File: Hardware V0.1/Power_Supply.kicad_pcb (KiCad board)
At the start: 2 copper layers, 100 x 50 mm, 65 parts, among them J1 ICSP, J2 Conn_01x01, J3 Conn_01x01, J4 Screw_Terminal_01x02, J6 Conn_01x04, J7 Conn_01x04, SW1 UP, SW2 DW, SW3 V/I, SW4 O_EN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

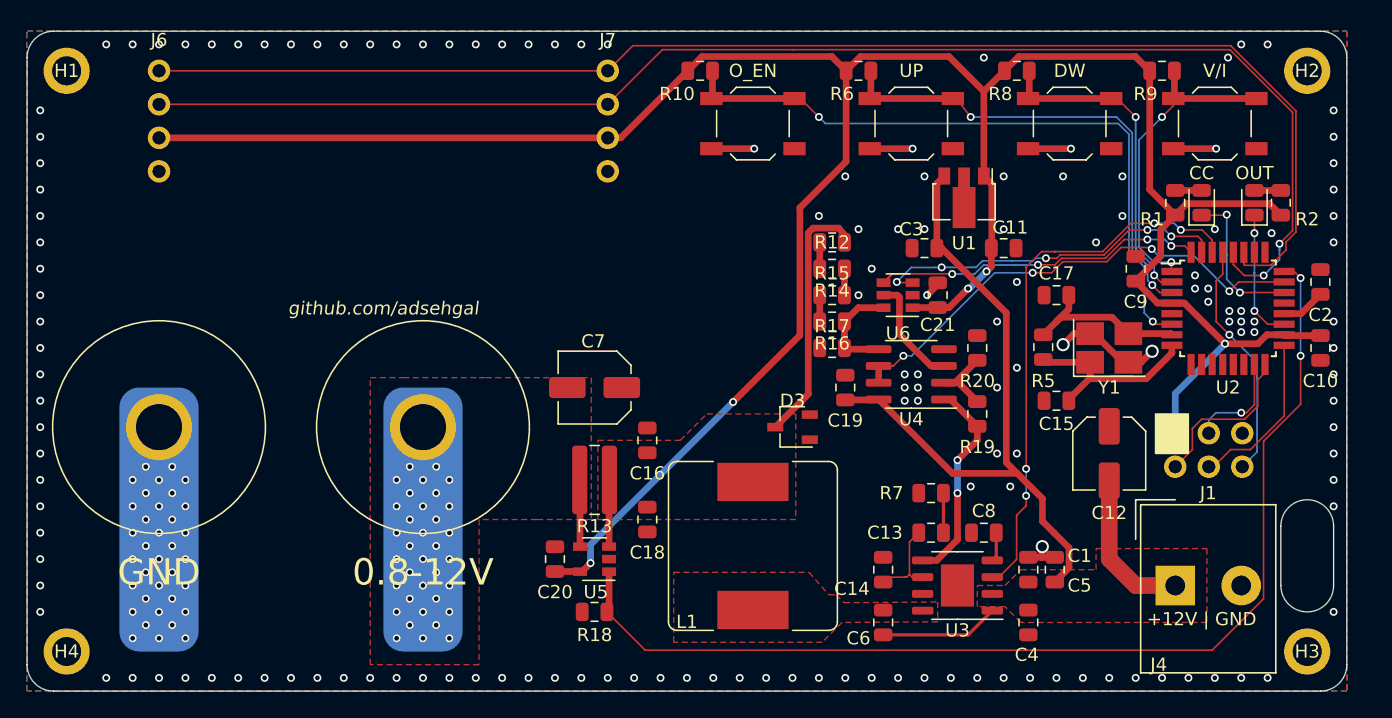
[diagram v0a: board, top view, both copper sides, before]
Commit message: placed all components
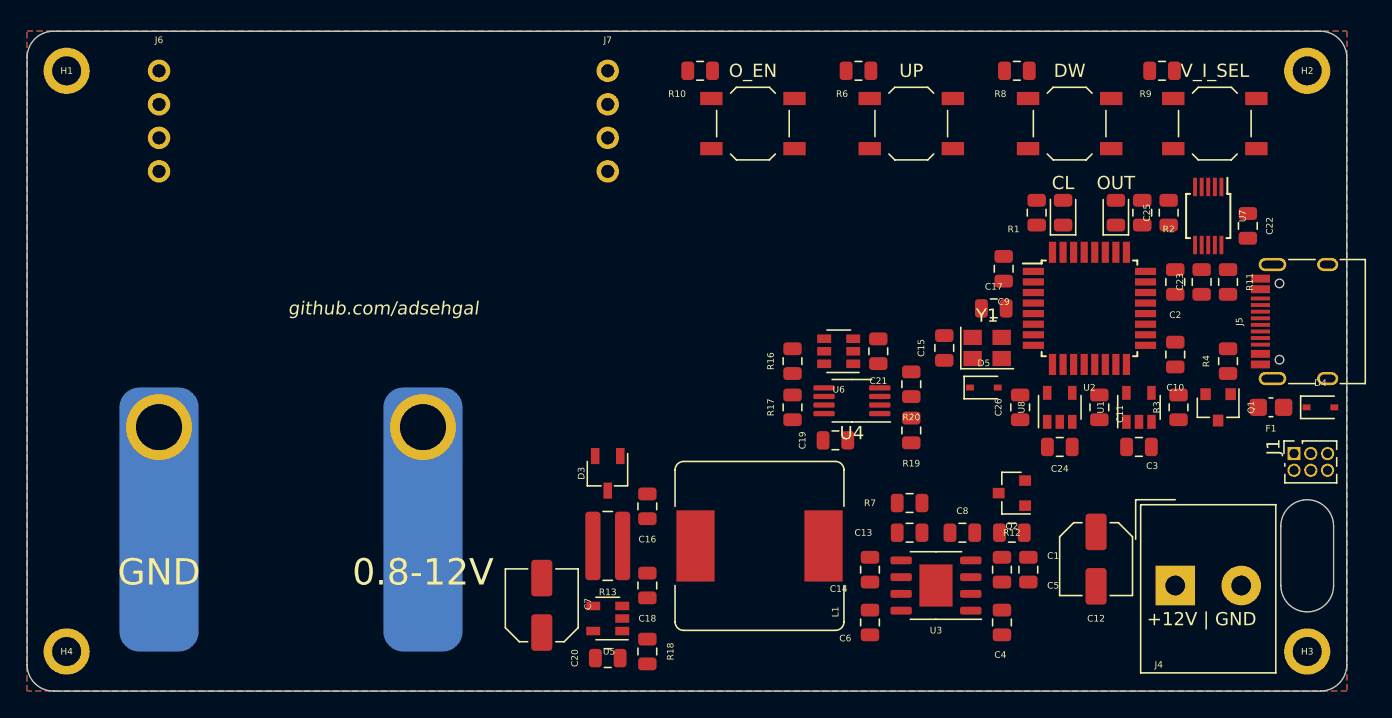
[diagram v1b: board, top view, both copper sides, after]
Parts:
- removed the G*** at (39.0, 29.0) (x2)
- removed R14, R15: 1.5K, Resistor_SMD:R_0805_2012Metric
- removed R5: 1M, Resistor_SMD:R_0805_2012Metric
- added C22: 100nF, Capacitor_SMD:C_0805_2012Metric, F.Cu at (104.5, 26.8)
- added C23: 100nF, Capacitor_SMD:C_0805_2012Metric, F.Cu at (101.0, 31.0)
- added C24: 100nF, Capacitor_SMD:C_0805_2012Metric, F.Cu at (90.2, 43.5)
- added C25: 100nF, Capacitor_SMD:C_0805_2012Metric, F.Cu at (98.5, 25.8)
- added C26: 1µF, Capacitor_SMD:C_0805_2012Metric, F.Cu at (87.2, 40.5)
- added D4: CUS10S30, Diode_SMD:D_SOD-323, F.Cu at (110.0, 40.5)
- added D5: CUS10S30, Diode_SMD:D_SOD-323, F.Cu at (84.5, 39.0)
- added F1: MF-PSMF020X-2, Fuse:Fuse_0805_2012Metric_Castellated, F.Cu at (106.2, 40.5)
- added G***: LOGO, LOGO, F.Cu at (39.5, 29.0)
- added J5: USB_C_Receptacle_USB2.0, Connector_USB:USB_C_Receptacle_HRO_TYPE-C-31-M-12, F.Cu at (109.5, 34.0)
- added Q1: FDN335N, Package_TO_SOT_SMD:SOT-23, F.Cu at (102.2, 40.5)
- added Q2: FDN335N, Package_TO_SOT_SMD:SOT-23, F.Cu at (86.6, 47.0)
- added R11: 5.1K, Resistor_SMD:R_0805_2012Metric, F.Cu at (103.0, 31.0)
- added R3: 10K, Resistor_SMD:R_0805_2012Metric, F.Cu at (99.2, 40.5)
- added R4: 5.1K, Resistor_SMD:R_0805_2012Metric, F.Cu at (103.0, 37.0)
- added U7: CH340E, Package_SO:MSOP-10_3x3mm_P0.5mm, F.Cu at (101.5, 26.0)
- added U8: MIC5205-3.3YM5, Package_TO_SOT_SMD:SOT-23-5, F.Cu at (90.2, 40.5)
- C11: value 100nF -> 1µF
- C20: value C_Small -> 100nF
- D1: value CC -> CL
- J1: footprint Custom_Vertical_2x_2.54mm_Pin_Header:PinHeader_2x03_P2.54mm_Vertical -> Connector_PinSocket_1.27mm:PinSocket_2x03_P1.27mm_Vertical
- R12: value 1K -> 10K
- R16: value 10K -> 14K
- SW3: value V/I -> V_I_SEL
- U1: value L78L08_SOT89 -> MIC5205-5.0YM5; footprint Package_TO_SOT_SMD:SOT-89-3 -> Package_TO_SOT_SMD:SOT-23-5
- U4: footprint Package_SO:SOIC-8_3.9x4.9mm_P1.27mm -> Package_SO:MSOP-8_3x3mm_P0.65mm
- Y1: footprint Crystal:Crystal_SMD_SeikoEpson_TSX3225-4Pin_3.2x2.5mm_HandSoldering -> Crystal:Crystal_SMD_SeikoEpson_TSX3225-4Pin_3.2x2.5mm
- moved R12 25.9 mm to (86.6, 50.0)
- moved C3 22.2 mm to (96.2, 43.5), turned to 180 degrees
- moved U1 20.7 mm to (96.2, 40.5), turned to 90 degrees
- moved C7 17.0 mm to (51.0, 55.5), turned to 90 degrees
- moved D3 14.4 mm to (56.0, 45.5), turned to -90 degrees
- moved C11 14.1 mm to (93.2, 40.5), turned to 90 degrees
- moved C10 11.0 mm to (99.0, 36.5)
- moved C2 11.0 mm to (99.0, 31.0)
- moved D1 10.5 mm to (90.5, 25.8)
- moved D2 10.5 mm to (94.5, 25.8)
- moved R1 10.5 mm to (88.5, 25.8)
- moved R2 10.5 mm to (96.5, 25.8)
- moved U2 10.5 mm to (92.5, 33.0)
- moved C9 10.0 mm to (86.0, 30.0)
- moved C15 9.39 mm to (81.5, 36.0), turned to -90 degrees
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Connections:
- R12 pad 1: Net-(R12-Pad1) -> Net-(Q2-Pad3)
- R12 pad 2: Net-(C16-Pad2) -> +VSW
- R16 pad 2: Net-(R15-Pad1) -> Net-(C16-Pad2)
- U1 pad 1: +5V -> +VSW
- U1 pad 3: +VSW -> Net-(Q1-Pad3)
- U2 pad 10: Net-(U2-Pad10) -> /POT_U~D
- U2 pad 11: Net-(U2-Pad11) -> /~POT_CS
- U2 pad 12: Net-(U2-Pad12) -> (no net)
- U2 pad 13: Net-(U2-Pad13) -> (no net)
- U2 pad 14: /~SS -> (no net)
- U2 pad 25: Net-(U2-Pad25) -> (no net)
- U2 pad 26: Net-(U2-Pad26) -> (no net)
- U2 pad 30: /REG_EN -> /RX
- U2 pad 31: /POT_U~D -> /TX
- U2 pad 32: /~POT_CS -> (no net)
- U3 pad 3: /REG_EN -> Net-(Q2-Pad3)
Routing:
- net +5V: track 201.5 -> 0.00 mm, vias 5 -> 0
- net /SCL0: track 106.5 -> 0.00 mm, vias 2 -> 0
- net /SDA0: track 104.5 -> 0.00 mm
- net /I_SENSE: track 82.4 -> 0.00 mm, vias 2 -> 0
- net +VSW: track 63.3 -> 0.00 mm
- net /SW4: track 50.8 -> 0.00 mm, vias 2 -> 0
- net /REG_EN: track 41.9 -> 0.00 mm, vias 4 -> 0
- net /V_SENSE: track 37.4 -> 0.00 mm, vias 4 -> 0
- net /SW1: track 36.7 -> 0.00 mm, vias 2 -> 0
- net /POT_U~D: track 27.2 -> 0.00 mm, vias 5 -> 0
- net /~POT_CS: track 26.0 -> 0.00 mm, vias 4 -> 0
- net GND: track 24.7 -> 0.00 mm, vias 188 -> 0
- net Net-(C16-Pad2): track 24.5 -> 0.00 mm
- net /SW2: track 24.4 -> 0.00 mm, vias 2 -> 0
- net /SW3: track 24.2 -> 0.00 mm, vias 2 -> 0
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- removed copper zone on F.Cu, net +VSW
- removed copper zone on F.Cu, net Net-(C16-Pad2)
- removed copper zone on F.Cu, net Net-(C6-Pad2)
- removed copper zone on F.Cu, net VDC

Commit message: finished layout for PCB with USB
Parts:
- removed J1: ICSP, Connector_PinSocket_1.27mm:PinSocket_2x03_P1.27mm_Vertical
- added D6: CUS10S30, Diode_SMD:D_SOD-323, B.Cu at (79.8, 42.5)
- added D7: CUS10S30, Diode_SMD:D_SOD-323, B.Cu at (78.0, 33.2)
- added TP1: TestPoint, TestPoint:TestPoint_Pad_D1.0mm, B.Cu at (88.0, 34.0)
- added TP2: TestPoint, TestPoint:TestPoint_Pad_D1.0mm, B.Cu at (90.0, 34.0)
- added TP3: TestPoint, TestPoint:TestPoint_Pad_D1.0mm, B.Cu at (92.0, 34.0)
- added TP4: TestPoint, TestPoint:TestPoint_Pad_D1.0mm, B.Cu at (88.0, 32.0)
- added TP5: TestPoint, TestPoint:TestPoint_Pad_D1.0mm, B.Cu at (90.0, 32.0)
- added TP6: TestPoint, TestPoint:TestPoint_Pad_D1.0mm, B.Cu at (92.0, 32.0)
- C10, C11, C13, C14, C15, C17, C19, C2, C21, C22, C23, C24, C26, C3, C8, C9, D5, R1, R11, R12, R2, R3, R4, R7: moved to B.Cu
- moved C24 22.2 mm to (80.5, 23.5)
- moved C22 18.1 mm to (86.5, 25.0)
- moved C23 17.6 mm to (84.5, 25.0)
- moved U8 17.1 mm to (80.5, 26.5), turned to -90 degrees
- moved C26 12.9 mm to (80.5, 29.5), turned to 0 degrees
- moved D1 11.0 mm to (101.5, 25.0)
- moved D2 11.0 mm to (105.5, 25.0)
- moved R1 11.0 mm to (99.5, 25.0)
- moved R2 11.0 mm to (107.5, 25.0)
- moved U7 10.0 mm to (91.5, 25.0), turned to 180 degrees
- moved U6 9.37 mm to (67.0, 29.5)
- moved R16 9.22 mm to (63.0, 31.0)
- moved R17 9.22 mm to (63.0, 34.5)
- moved C21 9.03 mm to (70.5, 29.5)
- moved U4 8.85 mm to (68.0, 34.0)
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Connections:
- U2 pad 10: /POT_U~D -> /~POT_CS
- U2 pad 11: /~POT_CS -> /POT_U~D
- U2 pad 23: /V_SENSE -> /I_SENSE
- U2 pad 24: /I_SENSE -> /V_SENSE
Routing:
- net +5V: track 0.00 -> 292.5 mm, vias 0 -> 15
- net /SCL0: track 0.00 -> 84.1 mm, vias 0 -> 2
- net /SDA0: track 0.00 -> 83.6 mm, vias 0 -> 2
- net +VSW: track 0.00 -> 65.9 mm, vias 0 -> 3
- net /I_SENSE: track 0.00 -> 62.8 mm, vias 0 -> 2
- net /REG_EN: track 0.00 -> 48.8 mm, vias 0 -> 1
- net /SW4: track 0.00 -> 39.6 mm
- net /V_SENSE: track 0.00 -> 35.8 mm, vias 0 -> 2
- net /SW3: track 0.00 -> 34.7 mm
- net /~POT_CS: track 0.00 -> 32.9 mm
- net /SW1: track 0.00 -> 31.8 mm
- net /POT_U~D: track 0.00 -> 31.1 mm
- net /SW2: track 0.00 -> 25.0 mm
- net Net-(C16-Pad2): track 0.00 -> 24.2 mm
- net /V_FB: track 0.00 -> 21.1 mm
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- added copper zone on F.Cu, net +VSW
- added copper zone on F.Cu, net Net-(C16-Pad2)
- added copper zone on F.Cu, net Net-(C6-Pad2)
- added copper zone on F.Cu, net VDC
